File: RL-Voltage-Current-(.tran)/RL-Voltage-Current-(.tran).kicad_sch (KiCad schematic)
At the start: 3 parts

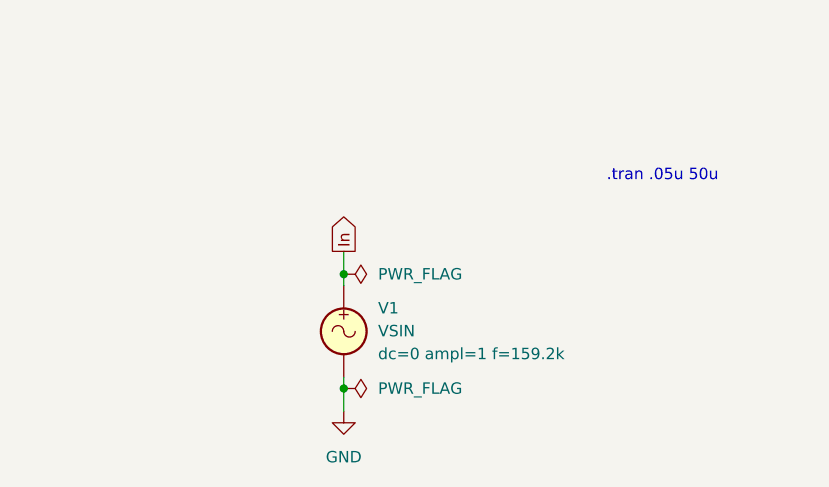
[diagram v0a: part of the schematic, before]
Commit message: Updated all schematics and prepared for KiCad 8.0
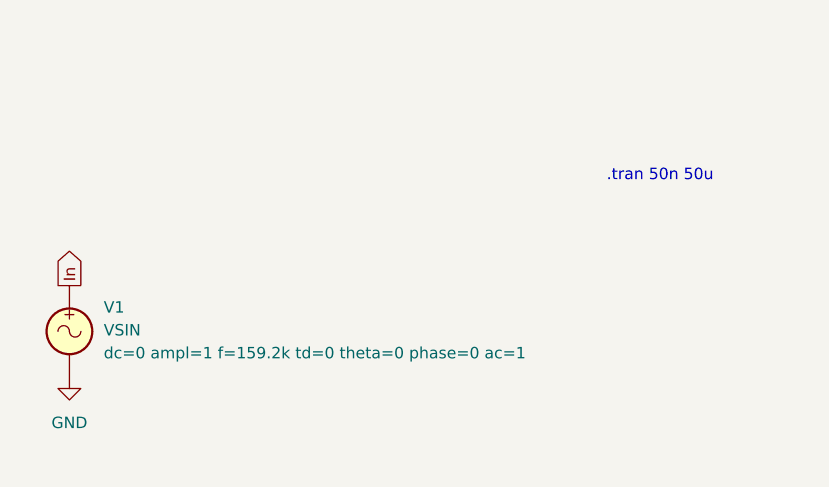
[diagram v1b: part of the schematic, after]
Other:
- note added: ".tran 50n 50u"
- note removed: ".tran .05u 50u"
